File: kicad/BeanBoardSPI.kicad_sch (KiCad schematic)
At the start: 39 parts, among them J1 Power, J10 SPI6, J11 GPO, J12 GPO, J13 GPI, J14 GPI, J15 Power, J2 Address, J3 Data / Control, J4 SPI0 (RA8875), J5 SPI1, J6 SPI2, J7 SPI3, J8 SPI4, J9 SPI5, U1 74HC244, U10 74HC138, U11 74HC165, U2 74HC164, U3 74HC165, U4 74HC373, U5 74HC165, U6 74HC165, U7 74HC04, U8 74HC02, U9 74HC74

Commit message: schematic
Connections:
- net GND: now also U7.5
- net SER_EN: no longer U7.5
- net ~{SER_EN}: now reaches U3.7 (~{Q7})
- net ~{SER_EN}: now also U8.2
- net at U7.6: no longer U8.2
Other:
- moved on the sheet: U7C
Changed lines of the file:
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@@
 	)
 	(junction
-		(at 167.64 120.65)
-		(diameter 0)
-		(color 0 0 0 0)
-	)
-	(junction
 		(at 6.35 66.04)
 		(diameter 0)
@@
 	)
 	(junction
-		(at 199.39 143.51)
-		(diameter 0)
-		(color 0 0 0 0)
-	)
-	(junction
 		(at 317.5 90.17)
 		(diameter 0)
@@
 	)
 	(no_connect
-		(at 345.44 85.09)
-	)
-	(no_connect
 		(at 151.13 12.7)
 	)
@@
 	)
 	(no_connect
+		(at 88.9 171.45)
+	)
+	(no_connect
 		(at 208.28 12.7)
 	)
@@
 	(wire
 		(pts
+			(xy 170.18 92.71) (xy 179.07 92.71)
+		)
+		(stroke
+			(width 0)
+			(type default)
+		)
+	)
+	(wire
+		(pts
 			(xy 309.88 167.64) (xy 320.04 167.64)
 		)
@@
 	(wire
 		(pts
-			(xy 80.01 11.43) (xy 85.09 11.43)
+			(xy 345.44 85.09) (xy 354.33 85.09)
 		)
 		(stroke
@@
 	(wire
 		(pts
-			(xy 6.35 116.84) (xy 6.35 129.54)
+			(xy 80.01 11.43) (xy 85.09 11.43)
 		)
 		(stroke
@@
 	(wire
 		(pts
-			(xy 170.18 130.81) (xy 199.39 130.81)
+			(xy 6.35 116.84) (xy 6.35 129.54)
 		)
 		(stroke
@@
 	(wire
 		(pts
-			(xy 199.39 130.81) (xy 199.39 143.51)
-		)
-		(stroke
-			(width 0)
-			(type default)
-		)
-	)
-	(wire
-		(pts
 			(xy 154.94 156.21) (xy 158.75 156.21)
 		)
@@
 	(wire
 		(pts
-			(xy 167.64 92.71) (xy 179.07 92.71)
-		)
-		(stroke
-			(width 0)
-			(type default)
-		)
-	)
-	(wire
-		(pts
 			(xy 312.42 157.48) (xy 320.04 157.48)
 		)
@@
 	(wire
 		(pts
-			(xy 167.64 140.97) (xy 168.91 140.97)
-		)
-		(stroke
-			(width 0)
-			(type default)
-		)
-	)
-	(wire
-		(pts
 			(xy 39.37 16.51) (xy 43.18 16.51)
 		)
@@
 	(wire
 		(pts
-			(xy 158.75 120.65) (xy 167.64 120.65)
-		)
-		(stroke
-			(width 0)
-			(type default)
-		)
-	)
-	(wire
-		(pts
 			(xy 80.01 102.87) (xy 73.66 102.87)
 		)
@@
 	(wire
 		(pts
-			(xy 170.18 97.79) (xy 170.18 130.81)
-		)
-		(stroke
-			(width 0)
-			(type default)
-		)
-	)
-	(wire
-		(pts
 			(xy 345.44 137.16) (xy 356.87 137.16)
 		)
@@
 	(wire
 		(pts
+			(xy 170.18 140.97) (xy 184.15 140.97)
+		)
+		(stroke
+			(width 0)
+			(type default)
+		)
+	)
+	(wire
+		(pts
 			(xy 158.75 149.86) (xy 158.75 129.54)
 		)
@@
 	(wire
 		(pts
-			(xy 167.64 120.65) (xy 167.64 140.97)
-		)
-		(stroke
-			(width 0)
-			(type default)
-		)
-	)
-	(wire
-		(pts
 			(xy 85.09 13.97) (xy 96.52 13.97)
 		)
@@
 	(wire
 		(pts
-			(xy 167.64 92.71) (xy 167.64 120.65)
-		)
-		(stroke
-			(width 0)
-			(type default)
-		)
-	)
-	(wire
-		(pts
 			(xy 154.94 139.7) (xy 154.94 156.21)
 		)
@@
 		)
 	)
+	(label "SER_EN"
+		(at 170.18 92.71 0)
+		(effects
+			(font
+				(size 1.27 1.27)
+			)
+			(justify left bottom)
+		)
+	)
 	(label "D2"
 		(at 134.62 88.9 180)
@@
 		)
 	)
+	(label "~{SER_EN}"
+		(at 354.33 85.09 180)
+		(effects
+			(font
+				(size 1.27 1.27)
+			)
+			(justify right bottom)
+		)
+	)
 	(label "GND"
 		(at 8.89 171.45 180)
@@
 		)
 	)
-	(label "SER_EN"
-		(at 158.75 120.65 0)
-		(effects
-			(font
-				(size 1.27 1.27)
-			)
-			(justify left bottom)
-		)
-	)
 	(label "+5V"
 		(at 246.38 10.16 0)
@@
 	)
 	(label "GND"
+		(at 73.66 171.45 180)
+		(effects
+			(font
+				(size 1.27 1.27)
+			)
+			(justify right bottom)
+		)
+	)
+	(label "GND"
 		(at 312.42 102.87 180)
 		(effects
@@
 		)
 	)
+	(label "~{SER_EN}"
+		(at 170.18 140.97 0)
+		(effects
+			(font
+				(size 1.27 1.27)
+			)
+			(justify left bottom)
+		)
+	)
 	(label "D0"
 		(at 238.76 82.55 0)
@@
 	(symbol
 		(lib_id "74xx:74HC04")
-		(at 176.53 140.97 0)
+		(at 81.28 171.45 0)
 		(unit 3)
 		(body_style 1)
@@
 		(dnp no)
 		(property "Reference" "U7"
-			(at 175.514 141.224 0)
+			(at 80.264 171.704 0)
 			(show_name no)
 			(do_not_autoplace no)
@@
 		)
 		(property "Value" "74HC04"
-			(at 179.07 136.398 0)
+			(at 83.82 166.878 0)
 			(show_name no)
 			(do_not_autoplace no)
@@
 		)
 		(property "Footprint" "Package_DIP:DIP-14_W7.62mm_Socket"
-			(at 176.53 140.97 0)
+			(at 81.28 171.45 0)
 			(hide yes)
 			(show_name no)
@@
 		)
 		(property "Datasheet" "https://assets.nexperia.com/documents/data-sheet/74HC_HCT04.pdf"
-			(at 176.53 140.97 0)
+			(at 81.28 171.45 0)
 			(hide yes)
 			(show_name no)
@@
 		)
 		(property "Description" "Hex Inverter"
-			(at 176.53 140.97 0)
+			(at 81.28 171.45 0)
 			(hide yes)
 			(show_name no)

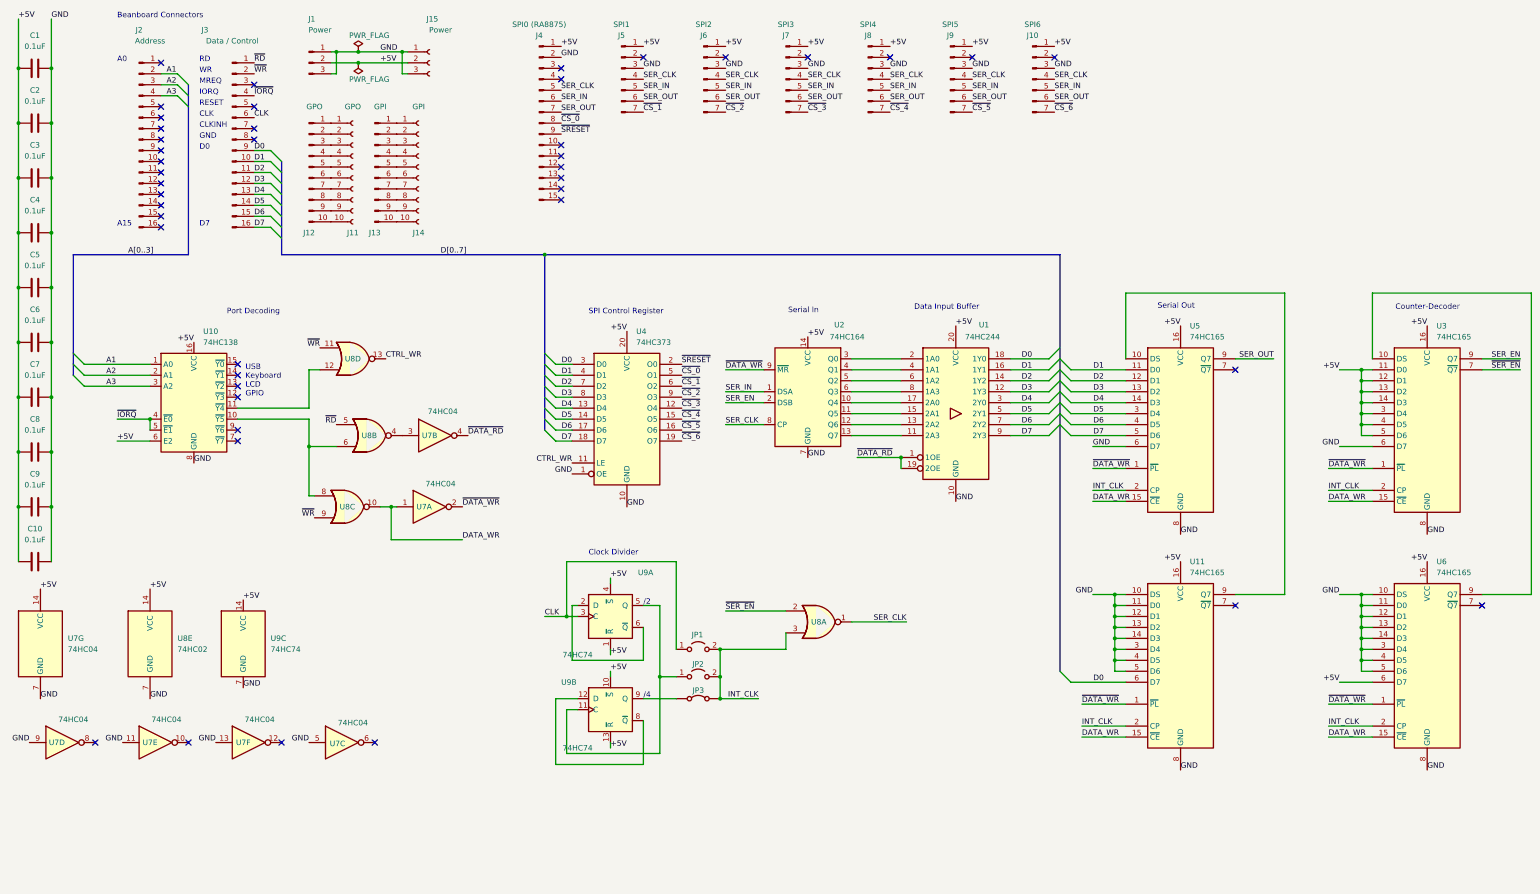
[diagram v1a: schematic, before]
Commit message: Update BeanBoardSPI.kicad_sch
added status input buffer and port decoding logic
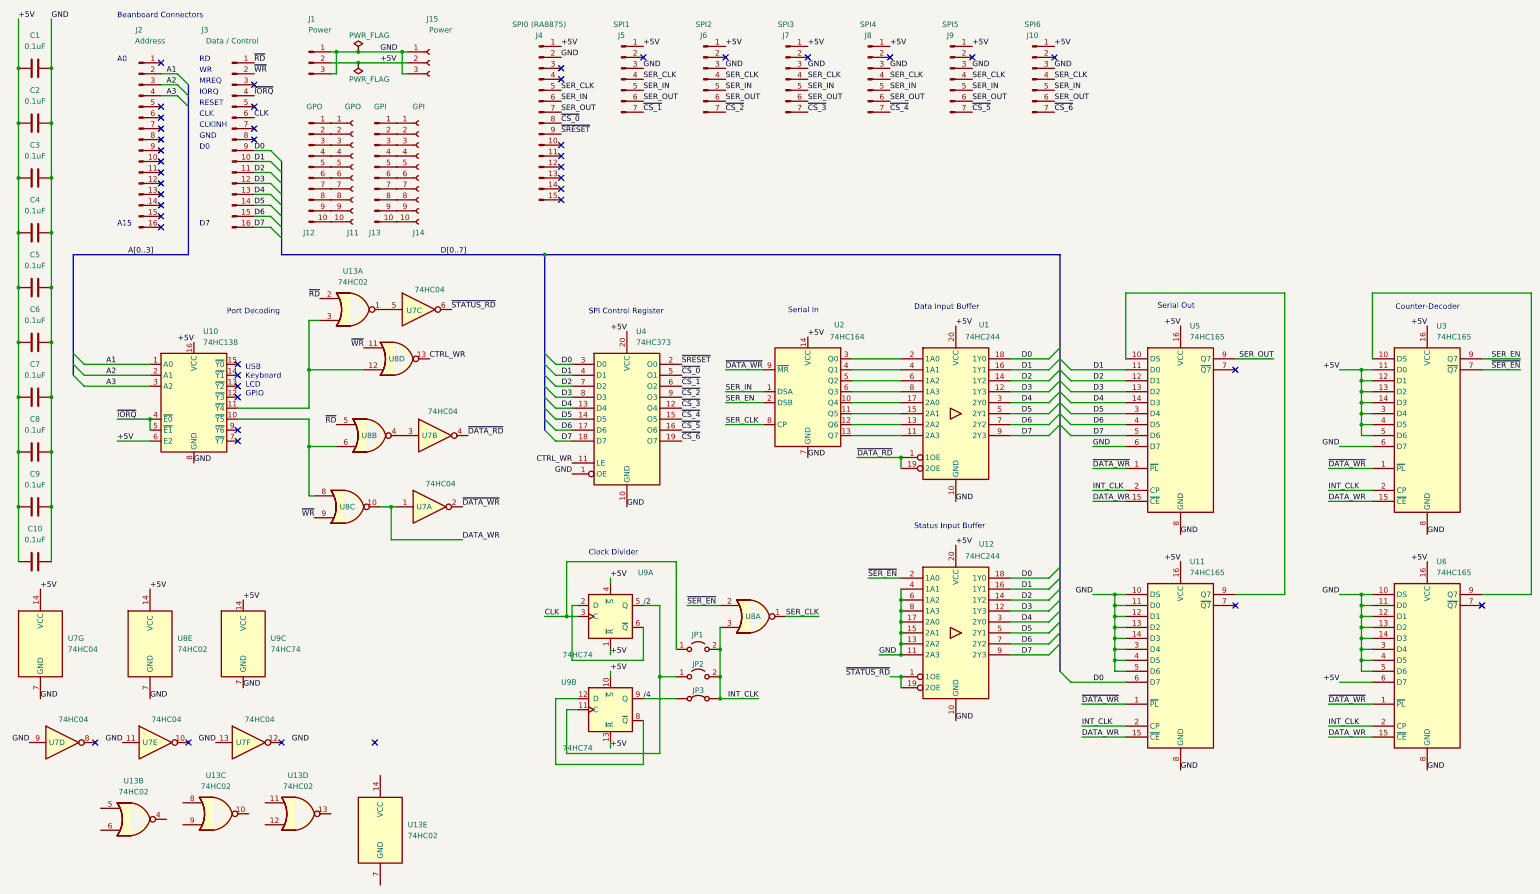
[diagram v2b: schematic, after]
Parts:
- added U12: 74HC244, symbol 74xx:74HC244
- added U13: 74HC02, symbol 74xx:74HC02
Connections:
- net +5V: now also U12.20 (VCC)
- net D0: now also U12.18 (1Y0)
- net D1: now also U12.16 (1Y1)
- net D2: now also U12.14 (1Y2)
- net D3: now also U12.12 (1Y3)
- net D4: now also U12.3 (2Y0)
- net D5: now also U12.5 (2Y1)
- net D6: now also U12.7 (2Y2)
- net D7: now also U12.9 (2Y3)
- net GND: now also U12.10 (GND), U12.11 (2A3), U12.13 (2A2), U12.15 (2A1), U12.17 (2A0), U12.4 (1A1), U12.6 (1A2), U12.8 (1A3); no longer U7.5
- net ~{RD}: now also U13.2
- net ~{SER_EN}: now also U12.2 (1A0)
- net at U10.11 (~{Y4}), U8.12: now also U13.3
- net ~{STATUS_RD}: now reaches U7.6
- net ~{STATUS_RD}: now also U12.1 (1OE), U12.19 (2OE)
- new net: U13.1, U7.5
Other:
- note added: "Status Input Buffer"
- moved on the sheet: U7C, U8A, U8D

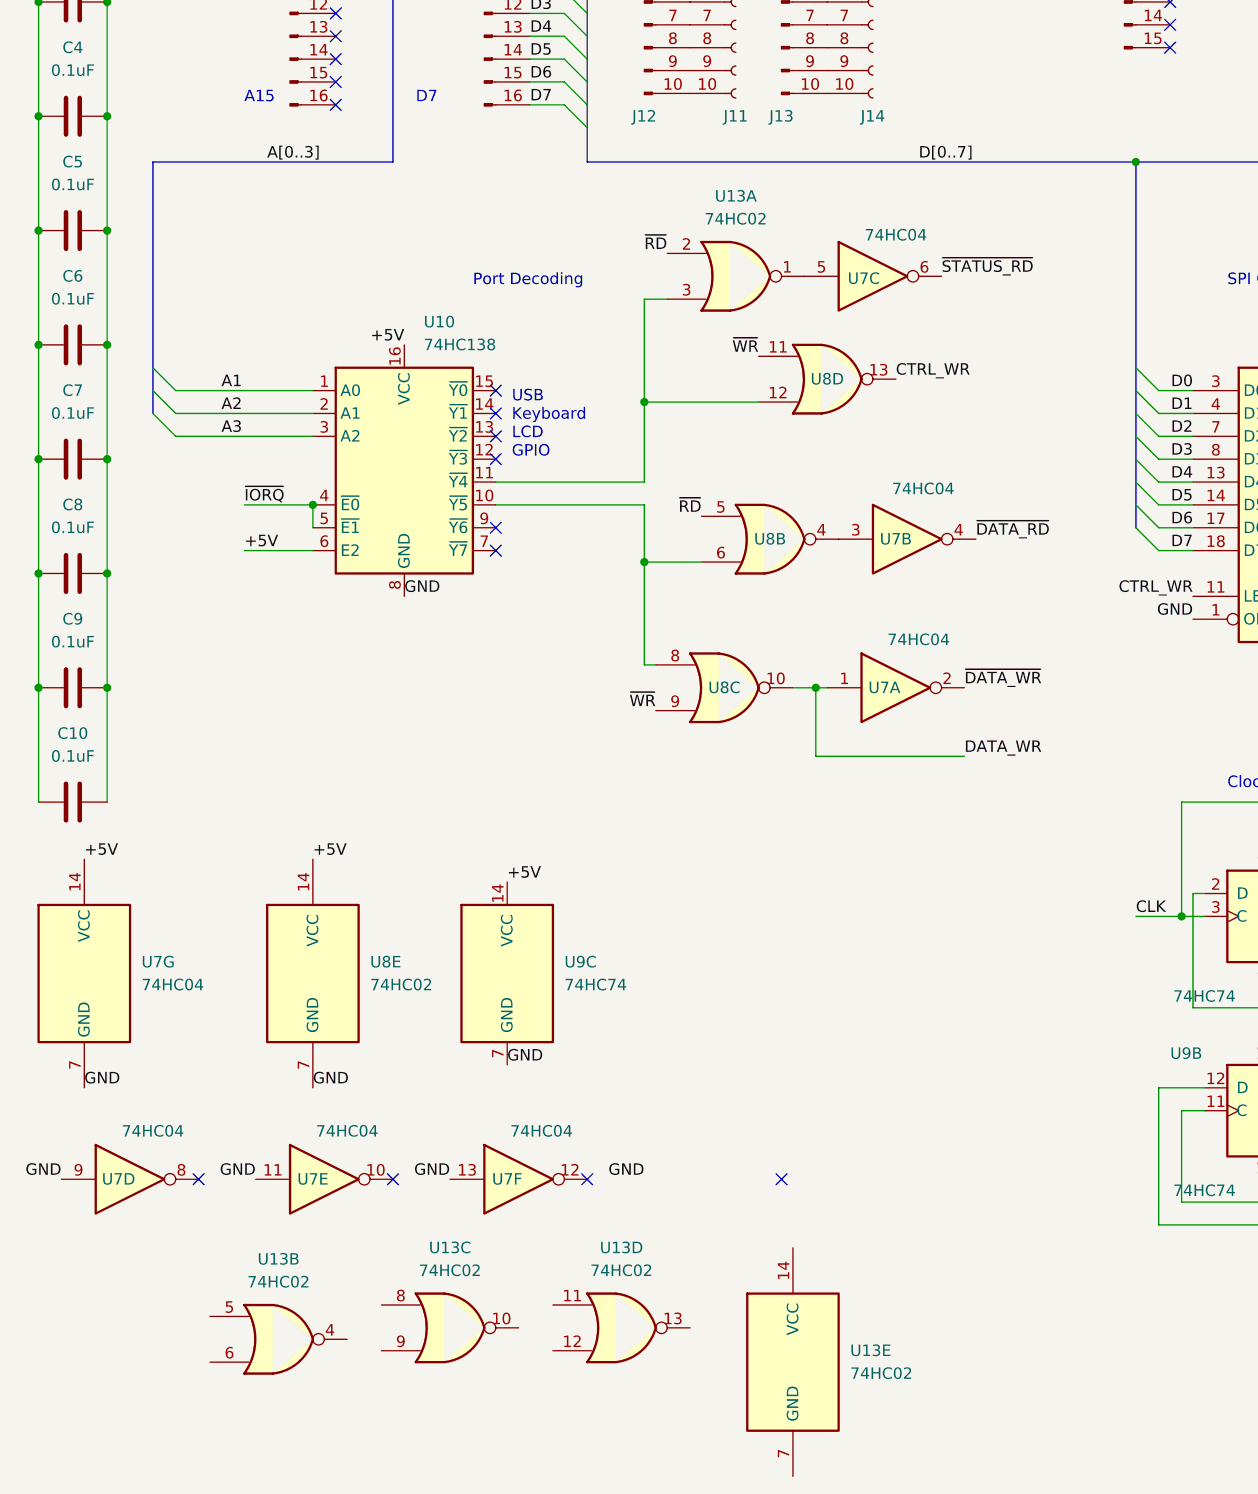
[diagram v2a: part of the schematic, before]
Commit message: rationalised fro chip count
replaced interters with NORs
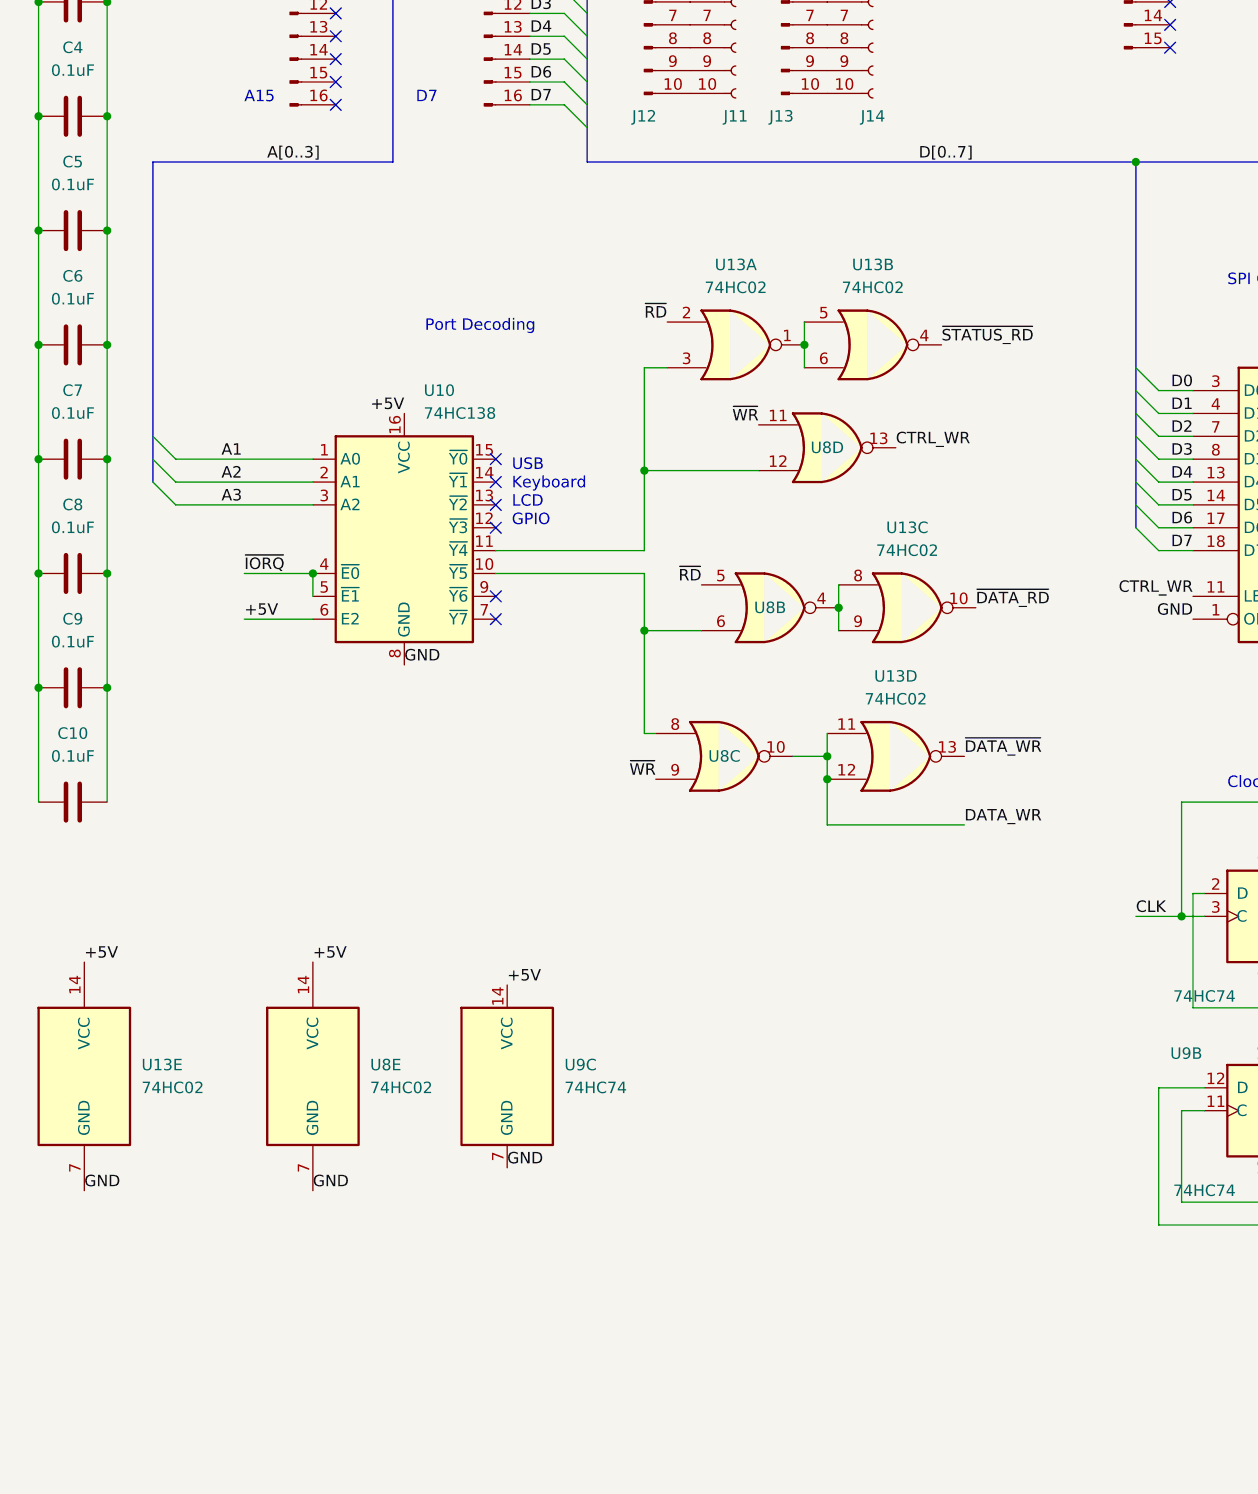
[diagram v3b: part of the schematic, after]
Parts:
- removed U7: 74HC04, Package_DIP:DIP-14_W7.62mm_Socket, symbol 74xx:74HC04
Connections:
- net +5V: now also U13.14 (VCC)
- net DATA_WR: now also U13.11, U13.12
- net GND: now also U13.7 (GND)
- net ~{DATA_RD}: now also U13.10
- net ~{DATA_WR}: now also U13.13
- net ~{STATUS_RD}: now also U13.4
- net at U8.4: now also U13.8, U13.9
- net at U13.5: now also U13.1, U13.6
- no-connect marks 44 -> 40
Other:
- moved on the sheet: U10, U13A, U13B, U13C, U13D, U13E, U8B, U8C, U8D, U8E, U9C
